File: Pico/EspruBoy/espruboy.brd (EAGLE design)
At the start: 41.3 x 55.1 mm, 10 parts, among them J1 JST-2P-SMD-PW-3410050P1

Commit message: watch bettery holder
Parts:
- added C2: (no value), rcl:C050-075X075
- added U$2: (no value), adafruit:CR2032-SMD
- C1: value (none) -> 1uF
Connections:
- new net N$3: C2.1, U$1.5V
- net BA: now also BTNA.1, BTNA.4
- net BB: now also BTNB.1, BTNB.4
- net BL: no longer BTNA.1, BTNA.4
- net BR: no longer BTNB.1, BTNB.4
- net GND: now also C2.2, U$2.-
- net N$2: now also U$2.+$1, U$2.+$2
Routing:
- net GND: track 179.6 -> 8.33 mm, vias 3 -> 1
- net N$2: track 11.5 -> 86.4 mm
- net N$3: track 0.00 -> 35.5 mm, vias 0 -> 1
- net BA: track 0.00 -> 35.5 mm, vias 0 -> 1
- net BB: track 0.00 -> 27.0 mm, vias 0 -> 1
- net BR: track 69.9 -> 50.0 mm
- net BL: track 74.7 -> 60.8 mm, vias 3 -> 1
- net +3V3: track 27.9 -> 37.8 mm, vias 2 -> 1
- net BD: track 62.7 -> 56.5 mm
- net LCD_DI: track 6.63 -> 5.41 mm
- net LCD_RES: track 15.8 -> 14.7 mm
- net LCD_DC: track 7.79 -> 6.70 mm
- net BU: track 48.4 -> 47.5 mm
- net LCD_CK: track 9.80 -> 8.93 mm
- net LCD_CE: track 12.1 -> 11.5 mm
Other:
- board text added: "EspruBoy"
- board text added: "www.espruino.com"

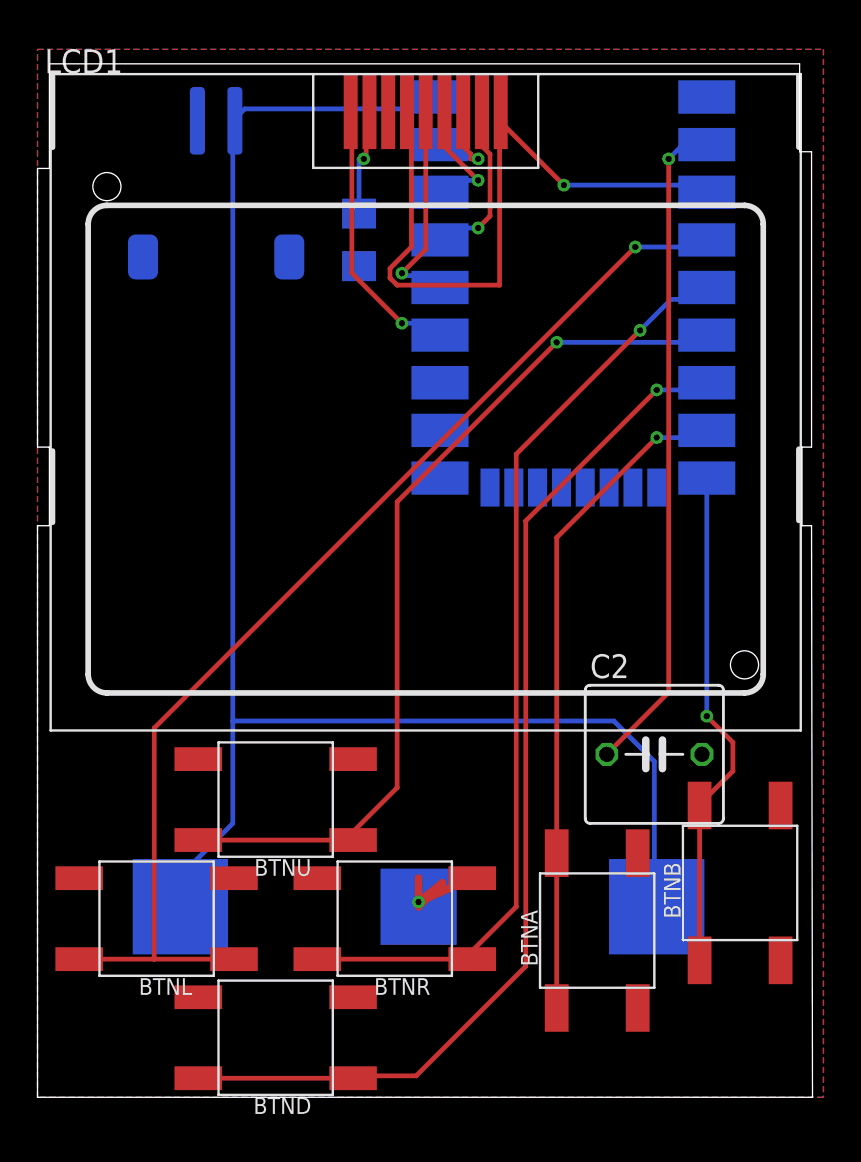
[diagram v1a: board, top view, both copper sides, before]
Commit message: added ESP12 shim
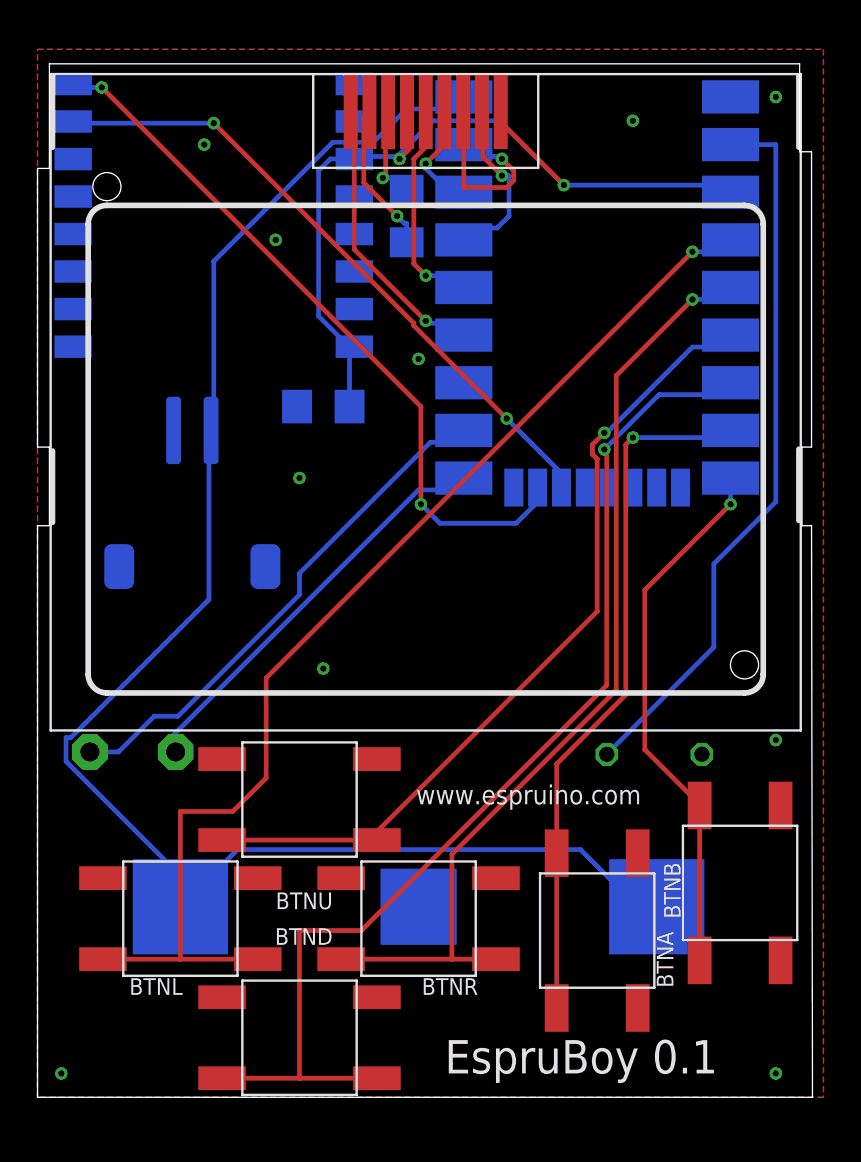
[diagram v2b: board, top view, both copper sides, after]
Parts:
- added C3: 10uF, rcl:C1206
- added ESP12: (no value), adafruit:ESP-12
- added SP1: SPEAKER/AL11P, adafruit:AL11P
- moved J1 16.6 mm to (8.26, 30.5)
- moved C1 2.84 mm to (19.7, 47.0), turned to 90 degrees
- moved BTND 1.27 mm to (14.0, 3.17)
- moved BTNU 1.27 mm to (14.0, 15.9)
- moved BTNL 1.27 mm to (7.62, 9.53)
- moved BTNR 1.27 mm to (20.3, 9.53)
- moved U$1 1.27 mm to (29.8, 39.4)
- flipped C2 to the bottom, turned to 180 degrees
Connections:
- new net ESP_RX: ESP12.15, U$1.A2
- new net ESP_TX: ESP12.16, U$1.A3
- new net N$4: SP1.-, U$1.A6
- new net N$5: SP1.+, U$1.A5
- net +3V3: now also C3.1, ESP12.3, ESP12.8
- net GND: now also C3.2, ESP12.9
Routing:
- net ESP_TX: track 0.00 -> 38.8 mm, vias 0 -> 2
- net ESP_RX: track 0.00 -> 34.7 mm, vias 0 -> 2
- net N$4: track 0.00 -> 27.7 mm
- net N$5: track 0.00 -> 22.2 mm
- net +3V3: track 37.8 -> 46.7 mm, vias 1 -> 2
- net LCD_DI: track 5.41 -> 10.6 mm
- net BU: track 47.5 -> 44.1 mm
- net N$3: track 35.5 -> 38.7 mm, vias 1 -> 0
- net GND: track 8.33 -> 5.29 mm, vias 1 -> 11
- net BD: track 56.5 -> 58.8 mm
- net N$1: track 5.81 -> 8.11 mm
- net BA: track 35.5 -> 37.5 mm
- net BB: track 27.0 -> 28.8 mm
- net BR: track 50.0 -> 51.0 mm
- net LCD_DC: track 6.70 -> 6.00 mm
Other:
- board text added: "EspruBoy 0.1"
- board text removed: "EspruBoy"

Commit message: make tab big enough for LCD
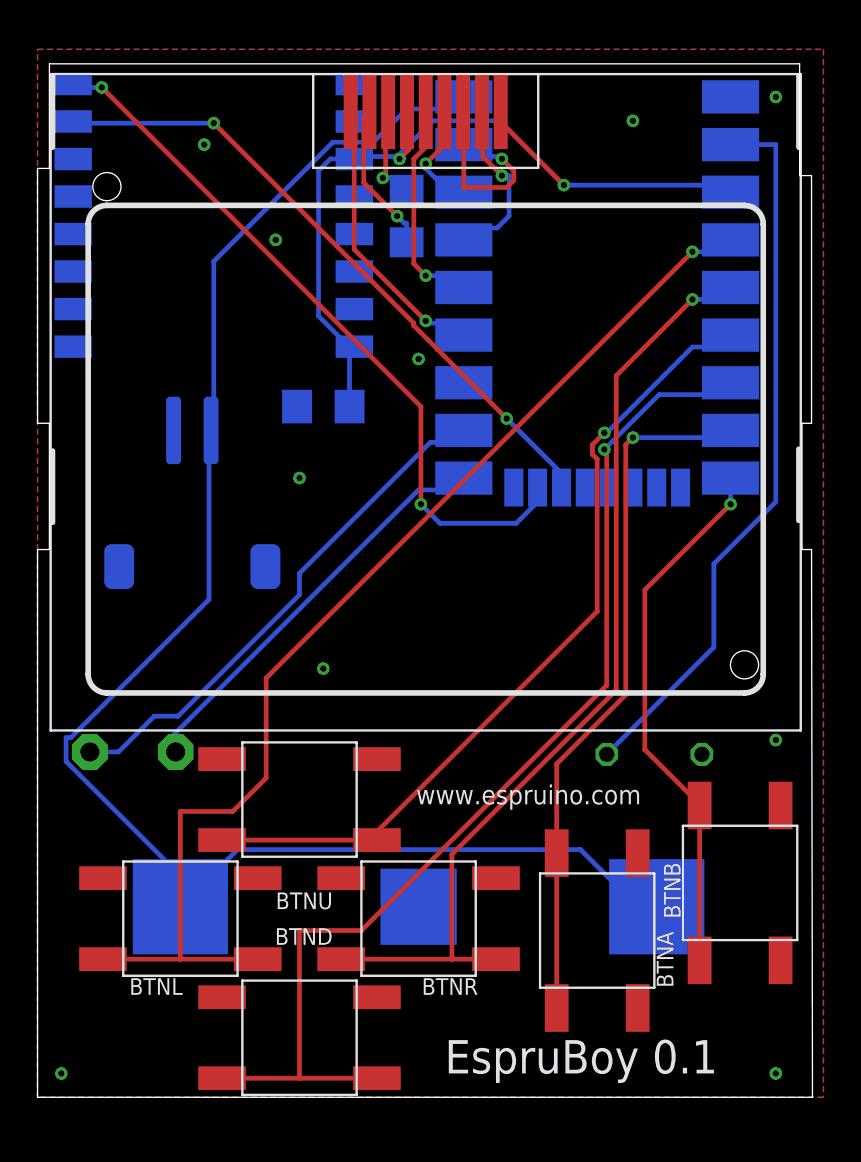
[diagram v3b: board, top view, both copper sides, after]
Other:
- outline, holes or cut-outs redrawn
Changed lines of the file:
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@@
 <plain>
 <wire x1="0" y1="0" x2="41.326" y2="0" width="0" layer="20"/>
-<wire x1="41.326" y1="0" x2="41.275" y2="30.48" width="0" layer="20"/>
-<wire x1="41.275" y1="30.48" x2="40.767" y2="30.48" width="0" layer="20"/>
-<wire x1="40.767" y1="30.48" x2="40.767" y2="34.671" width="0" layer="20"/>
-<wire x1="40.767" y1="34.671" x2="41.275" y2="34.671" width="0" layer="20"/>
-<wire x1="41.275" y1="34.671" x2="41.275" y2="50.419" width="0" layer="20"/>
-<wire x1="41.275" y1="50.419" x2="40.64" y2="50.419" width="0" layer="20"/>
-<wire x1="40.64" y1="50.419" x2="40.64" y2="55.108" width="0" layer="20"/>
+<wire x1="41.326" y1="0" x2="41.275" y2="29.21" width="0" layer="20"/>
+<wire x1="41.275" y1="29.21" x2="40.767" y2="29.21" width="0" layer="20"/>
+<wire x1="40.767" y1="29.21" x2="40.767" y2="35.941" width="0" layer="20"/>
+<wire x1="40.767" y1="35.941" x2="41.275" y2="35.941" width="0" layer="20"/>
+<wire x1="41.275" y1="35.941" x2="41.275" y2="49.149" width="0" layer="20"/>
+<wire x1="41.275" y1="49.149" x2="40.64" y2="49.149" width="0" layer="20"/>
+<wire x1="40.64" y1="49.149" x2="40.64" y2="55.108" width="0" layer="20"/>
 <wire x1="40.64" y1="55.108" x2="0.635" y2="55.108" width="0" layer="20"/>
 <wire x1="0.635" y1="55.108" x2="0.635" y2="49.53" width="0" layer="20"/>
 <wire x1="0.635" y1="49.53" x2="0" y2="49.53" width="0" layer="20"/>
-<wire x1="0" y1="49.53" x2="0" y2="34.671" width="0" layer="20"/>
-<wire x1="0" y1="34.671" x2="0.635" y2="34.671" width="0" layer="20"/>
-<wire x1="0.635" y1="34.671" x2="0.635" y2="30.48" width="0" layer="20"/>
-<wire x1="0.635" y1="30.48" x2="0" y2="30.48" width="0" layer="20"/>
-<wire x1="0" y1="30.48" x2="0" y2="0" width="0" layer="20"/>
+<wire x1="0" y1="49.53" x2="0" y2="35.941" width="0" layer="20"/>
+<wire x1="0" y1="35.941" x2="0.635" y2="35.941" width="0" layer="20"/>
+<wire x1="0.635" y1="35.941" x2="0.635" y2="29.21" width="0" layer="20"/>
+<wire x1="0.635" y1="29.21" x2="0" y2="29.21" width="0" layer="20"/>
+<wire x1="0" y1="29.21" x2="0" y2="0" width="0" layer="20"/>
 <text x="21.717" y="1.27" size="1.778" layer="25">EspruBoy 0.1</text>
 <text x="20.193" y="15.621" size="1.016" layer="25">www.espruino.com</text>

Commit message: fix shorted cr2032 battery connection
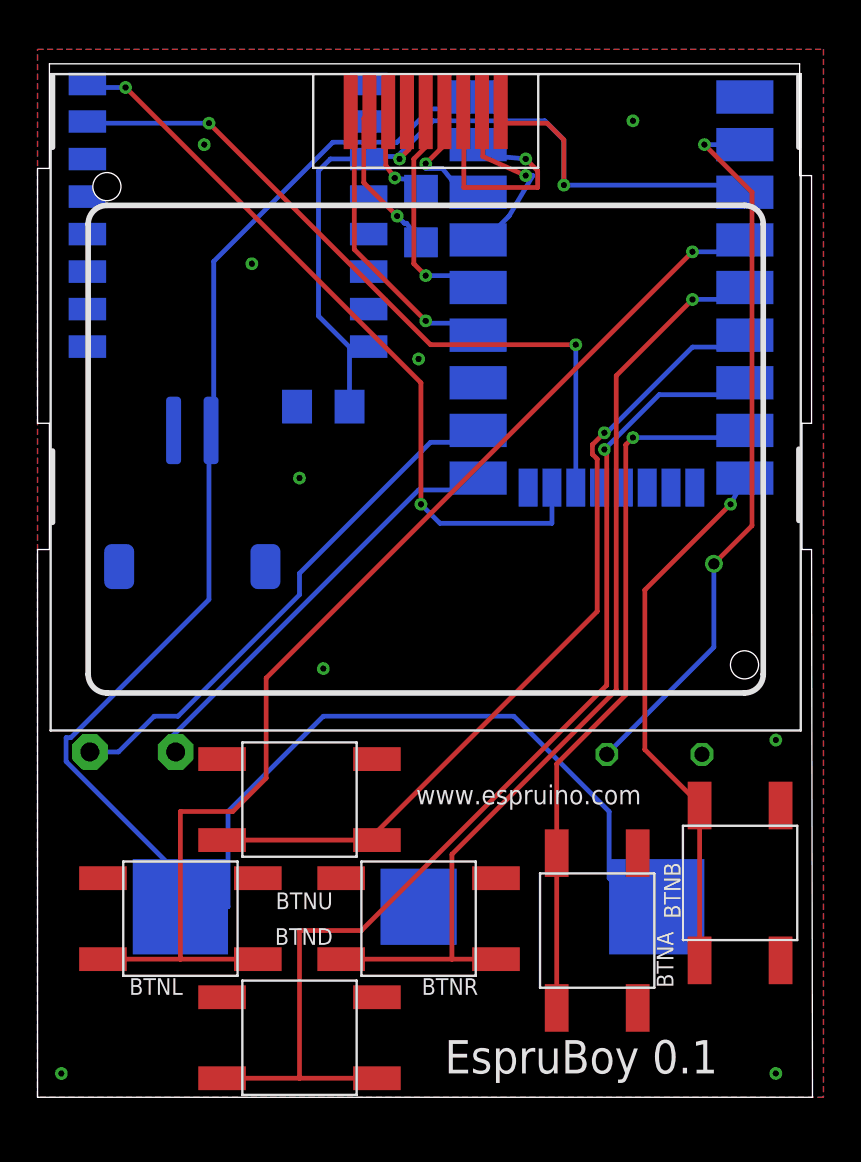
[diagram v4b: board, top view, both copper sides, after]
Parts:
- moved C1 0.76 mm to (20.4, 47.0)
- moved ESP12 0.76 mm to (10.2, 49.5)
- moved U$1 0.76 mm to (30.6, 39.4)
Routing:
- net N$2: track 86.0 -> 97.6 mm
- net +3V3: track 46.7 -> 53.0 mm
- net ESP_RX: track 34.7 -> 40.1 mm
- net ESP_TX: track 38.8 -> 41.7 mm
- net LCD_DI: track 10.6 -> 13.1 mm
- net LCD_CK: track 9.32 -> 10.5 mm
- net LCD_DC: track 6.00 -> 6.68 mm
- net BA: track 37.5 -> 38.1 mm
- net BD: track 58.8 -> 59.4 mm
- net LCD_RES: track 15.2 -> 15.8 mm
- net LCD_CE: track 11.6 -> 12.2 mm
- net N$4: track 27.7 -> 28.3 mm
- net N$5: track 22.2 -> 22.8 mm
- net BU: track 44.1 -> 44.8 mm
- net BR: track 51.0 -> 51.7 mm
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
